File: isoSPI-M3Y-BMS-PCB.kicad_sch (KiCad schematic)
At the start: 424 parts, among them J1 Screw_Terminal_01x04, J10 Screw_Terminal_01x04, J11 Screw_Terminal_01x03, J12 Screw_Terminal_01x08, J13 Conn_02x10_Odd_Even, J14 Screw_Terminal_01x04, J15 USB_C_Receptacle_USB2.0_16P, J16 Conn_01x03, J17 USB_C_Receptacle_USB2.0_16P, J18 USB_C_Receptacle_USB2.0_16P, J2 Conn_02x10_Odd_Even, J3 8P8C_LED_Shielded_x2, J5 OEM Shunt Connector, J6 349128020, J7 OEM HV Sense Connector, J8 OEM Connector, J9 Conn_01x03, K10 FC Positive, K11 FC Negative, K12 Link Negative, K13 Inverter, K14 Link Positive, K15 Link Negative, K16 FC Positive, K17 FC Negative, K18 Inverter, K9 Link Positive, Q1 CRSM034N06L2, Q2 CRSM034N06L2, Q3 CRSM034N06L2, Q5 CRSM034N06L2, SW1 TS-1187A-B-A-B, SW2 TS-1187A-B-A-B, SW3 TS-1187A-B-A-B, SW4 TS-1187A-B-A-B, U1 SN74LV1T08DBVR, U10 LTV-217-B-G, U11 RP2354B, U12 ADS1115, U13 ISO1050DUB, U15 SN74LV1T08DBVR, U16 BatMan, U17 TPS5430DDAR, U2 ISO1540, U20 LTV-217-B-G, U21 AMS1117-3.3, U22 F0505S-1WR3, U23 SN74LV1T08DBVR, U24 F0505S-1WR3, U25 SN74LV1T08DBVR, U26 SN74LV1T08DBVR, U27 RP2354B, U28 AM26LV32EIDR, U29 B0505S-3WR2, U3 INA228, U30 ISO1540, U32 SP3485EN-L/TR, U4 ISO1540, U6 F0505S-1WR3, U8 LTV-217-B-G, U9 LTV-217-B-G, Y1 ABM8-272-T3, Y2 ABM8-272-T3

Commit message: more updates
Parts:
- added TP16, TP19: TestPoint_2Pole, BMS_Library:TestPoint_2Pads_Pitch2.54mm_Pad1.5_Drill1.0mm, symbol Connector:TestPoint_2Pole
- TP1, TP15, TP17, TP18, TP2, TP3, TP4, TP5, TP6, TP7, TP8, TP9: footprint bms:TestPoint_2Pads_Pitch2.54mm_Drill0.9mm -> BMS_Library:TestPoint_2Pads_Pitch2.54mm_Pad1.5_Drill1.0mm
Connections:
- net GND: now also TP15.1, TP16.1
- net IsoSPI RX Debug: now also TP16.2
- net Serial API RX: now also TP19.1
- net Serial API TX: now also TP19.2
- net Snooper Debug: now also TP15.2
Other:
- moved on the sheet: TP15

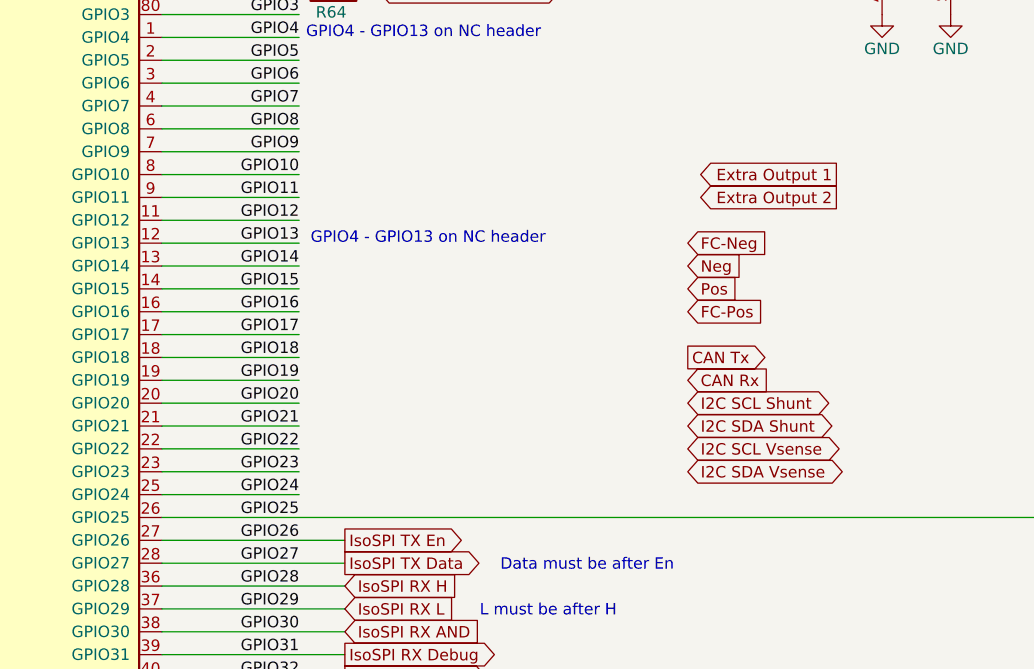
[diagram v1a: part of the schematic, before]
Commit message: connect remaining gpio
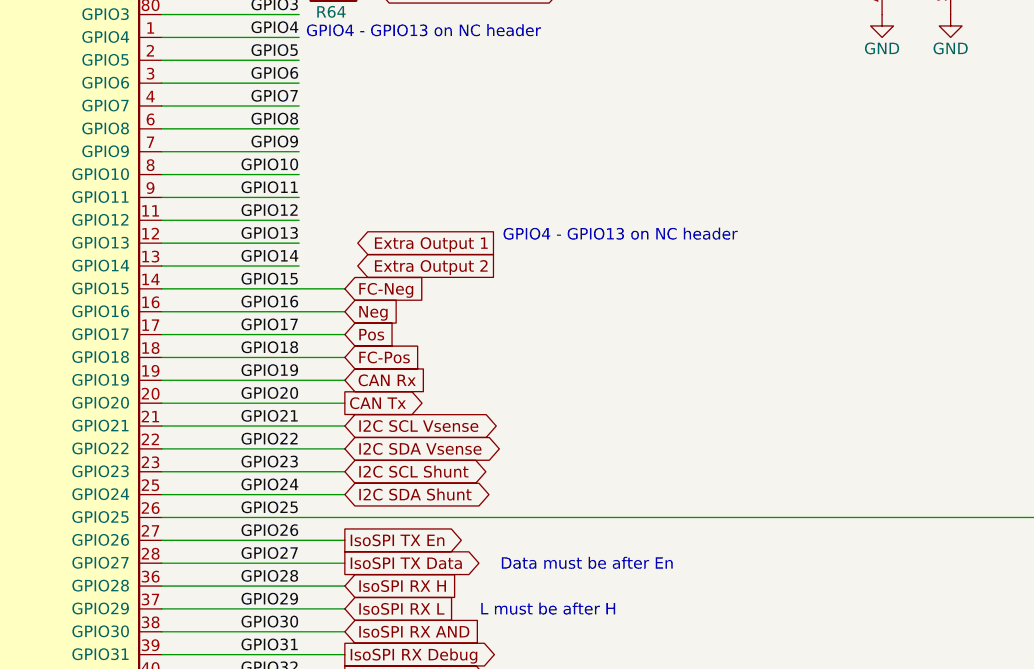
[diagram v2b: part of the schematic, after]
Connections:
- net GPIO15 is gone; now on net FC-Neg: U27.14 (GPIO15)
- net GPIO16 is gone; now on net Neg: U27.16 (GPIO16)
- net GPIO17 is gone; now on net Pos: U27.17 (GPIO17)
- net GPIO18 is gone; now on net FC-Pos: U27.18 (GPIO18)
- net GPIO19 is gone; now on net CAN Rx: U27.19 (GPIO19)
- net GPIO20 is gone; now on net CAN Tx: U27.20 (GPIO20)
- net GPIO21 is gone; now on net I2C SCL Vsense: U27.21 (GPIO21)
- net GPIO22 is gone; now on net I2C SDA Vsense: U27.22 (GPIO22)
- net GPIO23 is gone; now on net I2C SCL Shunt: U27.23 (GPIO23)
- net GPIO24 is gone; now on net I2C SDA Shunt: U27.25 (GPIO24)
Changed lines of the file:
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@@
 	(text "GPIO4 - GPIO13 on NC header"
 		(exclude_from_sim no)
-		(at 415.29 160.274 0)
+		(at 436.626 160.02 0)
 		(effects
 			(font
@@
 	(wire
 		(pts
-			(xy 398.78 187.96) (xy 414.02 187.96)
+			(xy 398.78 187.96) (xy 419.1 187.96)
 		)
 		(stroke
@@
 	(wire
 		(pts
-			(xy 398.78 180.34) (xy 414.02 180.34)
+			(xy 398.78 180.34) (xy 419.1 180.34)
 		)
 		(stroke
@@
 	(wire
 		(pts
-			(xy 398.78 175.26) (xy 414.02 175.26)
+			(xy 398.78 175.26) (xy 419.1 175.26)
 		)
 		(stroke
@@
 	(wire
 		(pts
-			(xy 398.78 182.88) (xy 414.02 182.88)
+			(xy 398.78 182.88) (xy 419.1 182.88)
 		)
 		(stroke
@@
 	(wire
 		(pts
-			(xy 398.78 172.72) (xy 414.02 172.72)
+			(xy 398.78 172.72) (xy 419.1 172.72)
 		)
 		(stroke
@@
 	(wire
 		(pts
-			(xy 398.78 170.18) (xy 414.02 170.18)
+			(xy 398.78 170.18) (xy 419.1 170.18)
 		)
 		(stroke
@@
 	(wire
 		(pts
-			(xy 398.78 165.1) (xy 414.02 165.1)
+			(xy 398.78 165.1) (xy 419.1 165.1)
 		)
 		(stroke
@@
 	(wire
 		(pts
-			(xy 398.78 185.42) (xy 414.02 185.42)
+			(xy 398.78 185.42) (xy 419.1 185.42)
 		)
 		(stroke
@@
 	(wire
 		(pts
-			(xy 398.78 167.64) (xy 414.02 167.64)
+			(xy 398.78 167.64) (xy 419.1 167.64)
 		)
 		(stroke
@@
 	(wire
 		(pts
-			(xy 398.78 177.8) (xy 414.02 177.8)
+			(xy 398.78 177.8) (xy 419.1 177.8)
 		)
 		(stroke
@@
 	(global_label "CAN Rx"
 		(shape input)
-		(at 457.2 175.26 0)
+		(at 419.1 175.26 0)
 		(fields_autoplaced yes)
 		(effects
@@
 		)
 		(property "Intersheetrefs" "${INTERSHEET_REFS}"
-			(at 467.14 175.26 0)
+			(at 429.04 175.26 0)
 			(effects
 				(font
@@
 	(global_label "Extra Output 2"
 		(shape output)
-		(at 473.71 154.94 180)
+		(at 435.61 162.56 180)
 		(fields_autoplaced yes)
 		(effects
@@
 		)
 		(property "Intersheetrefs" "${INTERSHEET_REFS}"
-			(at 456.5132 154.94 0)
+			(at 418.4132 162.56 0)
 			(effects
 				(font
@@
 	(global_label "FC-Pos"
 		(shape input)
-		(at 457.2 167.64 0)
+		(at 419.1 172.72 0)
 		(fields_autoplaced yes)
 		(effects
@@
 		)
 		(property "Intersheetrefs" "${INTERSHEET_REFS}"
-			(at 467.5633 167.64 0)
+			(at 429.4633 172.72 0)
 			(effects
 				(font
@@
 	(global_label "I2C SCL Shunt"
 		(shape bidirectional)
-		(at 457.2 177.8 0)
+		(at 419.1 185.42 0)
 		(fields_autoplaced yes)
 		(effects
@@
 		)
 		(property "Intersheetrefs" "${INTERSHEET_REFS}"
-			(at 475.2058 177.8 0)
+			(at 437.1058 185.42 0)
 			(effects
 				(font
@@
 	(global_label "Pos"
 		(shape input)
-		(at 457.2 165.1 0)
+		(at 419.1 170.18 0)
 		(fields_autoplaced yes)
 		(effects
@@
 		)
 		(property "Intersheetrefs" "${INTERSHEET_REFS}"
-			(at 463.6323 165.1 0)
+			(at 425.5323 170.18 0)
 			(effects
 				(font
@@
 	(global_label "Neg"
 		(shape input)
-		(at 457.2 162.56 0)
+		(at 419.1 167.64 0)
 		(fields_autoplaced yes)
 		(effects
@@
 		)
 		(property "Intersheetrefs" "${INTERSHEET_REFS}"
-			(at 463.7533 162.56 0)
+			(at 425.6533 167.64 0)
 			(effects
 				(font
@@
 	(global_label "Extra Output 1"
 		(shape output)
-		(at 473.71 152.4 180)
+		(at 435.61 160.02 180)
 		(fields_autoplaced yes)
 		(effects
@@
 		)
 		(property "Intersheetrefs" "${INTERSHEET_REFS}"
-			(at 456.5132 152.4 0)
+			(at 418.4132 160.02 0)
 			(effects
 				(font
@@
 	(global_label "CAN Tx"
 		(shape output)
-		(at 457.2 172.72 0)
+		(at 419.1 177.8 0)
 		(fields_autoplaced yes)
 		(effects
@@
 		)
 		(property "Intersheetrefs" "${INTERSHEET_REFS}"
-			(at 466.8376 172.72 0)
+			(at 428.7376 177.8 0)
 			(effects
 				(font
@@
 	(global_label "I2C SCL Vsense"
 		(shape bidirectional)
-		(at 457.2 182.88 0)
+		(at 419.1 180.34 0)
 		(fields_autoplaced yes)
 		(effects
@@
 		)
 		(property "Intersheetrefs" "${INTERSHEET_REFS}"
-			(at 476.2946 182.88 0)
+			(at 438.1946 180.34 0)
 			(effects
 				(font
@@
 	(global_label "I2C SDA Shunt"
 		(shape bidirectional)
-		(at 457.2 180.34 0)
+		(at 419.1 187.96 0)
 		(fields_autoplaced yes)
 		(effects
@@
 		)
 		(property "Intersheetrefs" "${INTERSHEET_REFS}"
-			(at 475.2663 180.34 0)
+			(at 437.1663 187.96 0)
 			(effects
 				(font
@@
 	(global_label "FC-Neg"
 		(shape input)
-		(at 457.2 160.02 0)
+		(at 419.1 165.1 0)
 		(fields_autoplaced yes)
 		(effects
@@
 		)
 		(property "Intersheetrefs" "${INTERSHEET_REFS}"
-			(at 467.6843 160.02 0)
+			(at 429.5843 165.1 0)
 			(effects
 				(font
@@
 	(global_label "I2C SDA Vsense"
 		(shape bidirectional)
-		(at 457.2 185.42 0)
+		(at 419.1 182.88 0)
 		(fields_autoplaced yes)
 		(effects
@@
 		)
 		(property "Intersheetrefs" "${INTERSHEET_REFS}"
-			(at 476.3551 185.42 0)
+			(at 438.2551 182.88 0)
 			(effects
 				(font

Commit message: rename serial
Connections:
- net GPIO14 is gone; now on net Extra Output 2: U27.13 (GPIO14)
- net MCU2_GPIO28 is gone; now on net IsoSPI RX H: U11.36 (GPIO28)
- net MCU2_GPIO29 is gone; now on net IsoSPI RX L: U11.37 (GPIO29)
- net MCU2_GPIO30 is gone; now on net IsoSPI RX AND: U11.38 (GPIO30)
- net MCU2_GPIO31 is gone; now on net IsoSPI RX Debug: U11.39 (GPIO31)
- net MCU2_GPIO32 is gone; now on net Snooper Debug: U11.40 (GPIO32)
- net Extra Output 1: now also U27.12 (GPIO13)
- net GPIO10: now also J2.16 (Pin_16); no longer J2.14 (Pin_14)
- net GPIO11: now also J2.18 (Pin_18); no longer J2.16 (Pin_16)
- net GPIO12: now also J2.20 (Pin_20); no longer J2.18 (Pin_18)
- net GPIO3: now also J2.2 (Pin_2)
- net GPIO4: now also J2.4 (Pin_4); no longer J2.2 (Pin_2)
- net GPIO5: now also J2.6 (Pin_6); no longer J2.4 (Pin_4)
- net GPIO6: now also J2.8 (Pin_8); no longer J2.6 (Pin_6)
- net GPIO7: now also J2.10 (Pin_10); no longer J2.8 (Pin_8)
- net GPIO8: now also J2.12 (Pin_12); no longer J2.10 (Pin_10)
- net GPIO9: now also J2.14 (Pin_14); no longer J2.12 (Pin_12)
- net GPIO1 renamed MAIN-SUP TX/RX
- net MAIN-SUP TX/RX: now also R64.1, TP9.2; no longer R63.2
- removed net GPIO13: J2.20 (Pin_20), U27.12 (GPIO13)
- net GPIO2 renamed MCU2_GPIO2
- net MCU2_GPIO2: now also U11.79 (GPIO2); no longer U27.79 (GPIO2)
- removed net MUC1-MCU2 TX-RX: R63.1, TP9.2, U11.79 (GPIO2)
- removed net MUC2-MCU1 TX-RX: R64.1, TP9.1, U11.78 (GPIO1)
- new net MCU2_GPIO1: R63.2, U11.78 (GPIO1)
- new net SUP-MAIN TX/RX: R63.1, TP9.1, U27.79 (GPIO2)
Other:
- note added: "GPIO3 - GPIO12 on NC header"
- note removed: "GPIO4 - GPIO13 on NC header"
- moved on the sheet: R59, R63, R64, TP9

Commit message: progress...
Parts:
- removed JP9: SolderJumper_3_Bridged12, Jumper:SolderJumper-3_P1.3mm_Bridged12_RoundedPad1.0x1.5mm_NumberLabels, symbol Jumper:SolderJumper_3_Bridged12
- added C76: 100nF, Capacitor_SMD:C_0603_1608Metric, symbol Device:C_Small
- added JP9: SolderJumper_2_Bridged, Jumper:SolderJumper-2_P1.3mm_Bridged_RoundedPad1.0x1.5mm, symbol Jumper:SolderJumper_2_Bridged
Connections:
- net GND_Shunt: now also C76.1
- net Serial API RX: now also J15.A7 (D-), J15.B7 (D-); no longer J15.A6 (D+), J15.B6 (D+)
- net Serial API TX: now also J15.A6 (D+), J15.B6 (D+); no longer J15.A7 (D-), J15.B7 (D-)
- net Shunt_5V: now also C76.2
- net at TR10.2 (C_TD): now also JP9.1 (A)
- net at C85.2: now also JP9.2 (B)
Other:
- moved on the sheet: D31, R79

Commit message: more routing
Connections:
- net +3V3 is gone; now on net +3.3V: C21.1, C22.2, C25.1, U1.5 (VCC), U28.16 (VDD), U28.4 (G), U32.8 (VCC)
- net GPIO11 is gone; now on net Emergency Stop: J2.18 (Pin_18), U27.9 (GPIO11)
- net GPIO12 is gone; now on net Extra Input: J2.20 (Pin_20), U27.11 (GPIO12)
- net MCU2_GPIO11 is gone; now on net Emergency Stop: J13.16 (Pin_16), U11.9 (GPIO11)
- net BatSPI_CS: no longer U16.58 (SPI_MISO), U27.44 (GPIO35)
- net CAN Rx: now also U27.20 (GPIO20); no longer U27.19 (GPIO19)
- net CAN Tx: now also U27.19 (GPIO19); no longer U27.20 (GPIO20)
- net FC-Pos: now also U27.16 (GPIO16); no longer U27.18 (GPIO18)
- net I2C SCL Vsense: now also U27.22 (GPIO22); no longer U27.21 (GPIO21)
- net I2C SDA Vsense: now also U27.21 (GPIO21); no longer U27.22 (GPIO22)
- net Neg: now also U27.17 (GPIO17); no longer U27.16 (GPIO16)
- net Pos: now also U27.18 (GPIO18); no longer U27.17 (GPIO17)
- new net BatSPI_MOSI: U16.57 (SPI_MOSI), U27.44 (GPIO35)
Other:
- moved on the sheet: D33, R48

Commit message: getting close!
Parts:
- removed C27: 4.7u, Capacitor_SMD:C_0402_1005Metric, symbol Device:C
- removed R50: 33r, Resistor_SMD:R_0402_1005Metric, symbol Device:R
- added C27, C90: 1uF, Capacitor_SMD:C_0603_1608Metric, symbol Device:C_Small
- added C77, C83, C84, C88: 100nF, Capacitor_SMD:C_0603_1608Metric, symbol Device:C_Small
- added D35: White, LED_SMD:LED_0805_2012Metric, symbol Device:LED
- added R50, R73: 10k, Resistor_SMD:R_0603_1608Metric_Pad0.98x0.95mm_HandSolder, symbol Device:R_Small
- added R71, R72: 1.8k, Resistor_SMD:R_0603_1608Metric, symbol Device:R_Small
- added R76: 24k, Resistor_SMD:R_0603_1608Metric, symbol Device:R_Small
- added TP20, TP21: TestPoint_2Pole, BMS_Library:TestPoint_2Pads_Pitch2.54mm_Pad1.5_Drill1.0mm, symbol Connector:TestPoint_2Pole
- added U5, U7: LTV-217-B-G, Package_SO:SSOP-4_4.4x2.6mm_P1.27mm, symbol Isolator:LTV-817S
- C26, C40: footprint Capacitor_SMD:C_0603_1608Metric_Pad1.08x0.95mm_HandSolder -> Capacitor_SMD:C_0603_1608Metric
- U22, U24, U6: footprint Converter_DCDC:Converter_DCDC_TRACO_TEA1-xxxxHI_THT -> BMS_Library:H0505S-1WR2
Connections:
- net +3.3V: now also R80.2, U5.4, U7.4
- net +5V: now also C27.2, C90.2, U5.1, U7.1
- net 3.3V Sense: now also C83.2
- net 5V Sense: now also C84.2
- net GND: now also J8.3 (Pin_3), J8.4 (Pin_4), C77.1, C83.1, C84.1, C88.1, D35.1 (K), R50.1, R73.1, TP20.1, TP21.1
- net HMI Serial RX: now also R34.1, U27.47 (GPIO38); no longer R35.1, U27.48 (GPIO39)
- net HMI Serial TX: now also R35.1, U27.48 (GPIO39); no longer R34.1, U27.47 (GPIO38)
- net IsoSPI RX Debug: no longer U11.39 (GPIO31)
- net Snooper Debug: no longer U11.40 (GPIO32)
- net VContactor Sense: now also C77.2
- net V_{Contactor}: now also R76.1
- net Vin Logic Sense: now also C88.2
- net 1/2 Vsense: now reaches C10.1, C41.2, C42.1, C43.2, C95.2, R228.2, R229.1, R40.2, R41.1, R45.2, R47.1
- net at J8.17 (Pin_17): now also R72.1
- net at J8.18 (Pin_18): now also R71.1
- net GPIO10 renamed FC-CTR-POS-AUX
- net FC-CTR-POS-AUX: now also R50.2, U5.3
- net GPIO9 renamed FC-CTR-NEG-AUX
- net FC-CTR-NEG-AUX: now also R73.2, U7.3
- new net: D35.2 (A), R76.2
- new net: C90.1, R72.2, U7.2
- new net: C27.1, R71.2, U5.2
- new net IsoSPI RX Debug 2: TP20.2, U11.39 (GPIO31)
- new net Snooper Debug 2: TP21.2, U11.40 (GPIO32)
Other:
- note added: "Specified DC-DC is a smaller package - put footprint will fit the 3KV or 6KV version"
- moved on the sheet: C26, C40, D18, D50, D51, J12, J3B, J8, R22, R23, R28, R29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

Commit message: progress
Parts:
- removed C69: 4.7u, Capacitor_SMD:C_0402_1005Metric, symbol Device:C
- removed R58: 33r, Resistor_SMD:R_0402_1005Metric, symbol Device:R
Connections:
- net +3.3V: now also R171.2
- net FC-CTR-NEG-AUX: now also J2.16 (Pin_16), U27.8 (GPIO10); no longer J2.14 (Pin_14), U27.7 (GPIO9)
- net FC-CTR-POS-AUX: now also J2.14 (Pin_14), U27.7 (GPIO9); no longer J2.16 (Pin_16), U27.8 (GPIO10)
